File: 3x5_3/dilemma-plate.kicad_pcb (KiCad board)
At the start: 2 copper layers, 134 x 95.1 mm, 24 parts, among them SW101 NA_SW_Push, SW102 NA_SW_Push, SW103 NA_SW_Push, SW104 NA_SW_Push, SW105 NA_SW_Push, SW106 NA_SW_Push, SW107 NA_SW_Push, SW108 NA_SW_Push, SW109 NA_SW_Push, SW112 NA_SW_Push, SW113 NA_SW_Push, SW114 NA_SW_Push, SW115 NA_SW_Push, SW116 NA_SW_Push, SW117 NA_SW_Push, SW118 NA_SW_Push, SW119 NA_SW_Push, SW3001 NA_SW_Push

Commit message: switchplate
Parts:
- added H111: NA_Mount, local-libraries:Tenting_Puck, B.Cu at (168.8, 59.2)
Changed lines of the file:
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@@
 		)
 		(group ""
-			(members "18a6017f-ffb6-468c-8ad2-d1e65c980797" "1e9dc653-d796-481e-916b-10005a3d162f"
-				"1fd756a0-f206-4082-b7b1-289f6806d907" "298fd9b2-c9c4-4fb9-807c-0fc8cd5b9cba"
-				"35375497-e94a-4f06-a222-bf7addb77599" "3b888a55-3c4c-41de-9f1a-ac9d52ed99d5"
-				"3e25eb27-7766-4408-993b-eabdf33a15bf" "431225ac-bd0e-4e08-a494-c40d164e2537"
-				"522cac54-0b11-4791-888c-e7ded3e0ca3d" "522d6815-39b9-461e-8790-dd977ede2398"
-				"5546a2ae-57d7-40bc-8d2e-3e6342b024a3" "56fc0188-a46c-4fea-85be-565f00de21f7"
-				"5b26266e-9816-4449-ae28-c63e9d40efc1" "6105f4c5-8b0d-40ea-9fff-03a51df45137"
-				"62fa6b5c-3e7a-47ea-8490-97169fca3748" "6d991e6b-c12e-49aa-97fe-81406dea6a0f"
-				"77ab767f-daca-4994-b1dc-09e0116332ce" "783291f6-c796-4002-8fba-8e5e8cd6a844"
-				"8028d15d-6b94-4461-b460-0e59a82dbef8" "8036b940-5d2f-47a3-92ce-c59f15daa10a"
-				"827b9336-2005-4876-91df-0b7e21506845" "888ccea9-396c-47db-8d12-6a158d271942"
-				"95e2d21a-c768-495e-ab0f-7fdc0561792a" "963e86f8-8028-43a5-a583-777a1a724f63"
-				"9725a7eb-fbad-4445-997b-6893073f64e4" "97797248-1ebb-4d67-9d40-7fa9f49aa101"
-				"a31a874a-10a9-4085-bb2e-7ae6c695fd1d" "a3d442e0-a006-4df3-9afb-74bad3d9074a"
-				"a6783e92-1c61-4fac-9a5e-fdf22107ddb4" "a6edc55a-221d-4ae6-bffb-877fa3f8255f"
-				"ab6da59e-c0c9-444f-ac9c-b41e1cc33cb7" "b2584371-f3ef-4b80-afc1-b0a9ac187e03"
-				"b791176a-09aa-49ba-aaf0-00d4e364508e" "be3320bc-3aa9-4157-b558-ef6af8c43c2e"
-				"c70f1618-31fa-4ea9-8e51-2fd3c1244cda" "cbf11959-a461-4afa-af92-5fb8a755fd74"
-				"d0f27782-a812-427e-a1fb-0f6bc1eb0358" "d61a1469-8a70-457c-a318-8e3a44313dac"
-				"d95e60d4-b23c-42c9-b0ee-c09b32c68f8e" "dcc2c6ab-cf55-4ea2-81b9-2faa12349492"
-				"e28f69b4-e63c-443d-b198-09082df40ac6" "e9561920-4c84-434b-bb06-192ef4388cd0"
-				"f6fa60ae-145d-4918-8f28-a70c0320631c" "fc3d7266-24b8-47f1-844e-45b49a9f565e"
+			(members "06fd2d42-9e3d-4690-9213-9cdc7a998e4e" "1578d53f-b03b-43ed-a1ee-80c129b84bd2"
+				"237d5ba1-f081-4609-a567-8f08e89e4127" "28eae3de-9e28-4a41-8eb8-48b5cdd89c41"
+				"294e80ac-4184-4ab5-9341-ffd47eff33fc" "2975c91c-a03c-473c-bd74-390e810a9597"
+				"29f52380-fb83-4aa3-a89f-b73e0a496111" "305da9ae-5ffd-4334-9232-f78d5d0c655c"
+				"30b917aa-8564-41ad-8b33-177330258a9c" "3e56117d-53eb-4852-b9c6-79d85b387bfd"
+				"43157336-987f-4d6d-b473-97e6e7ea65f8" "474277ff-e58b-42ca-8847-5ec2961336b0"
+				"4b58b3f7-d579-4dae-9ab5-2eadcf436765" "4e783968-626b-453f-9e8c-af5ce592b87f"
+				"5e36adeb-0ae9-4595-8625-8b71ac3db49f" "64f87574-665c-4c55-b142-3479ecc681e7"
+				"7b14f2b2-a3c5-4c18-b87d-7dc452cad28d" "816d5be3-ad1d-4093-8293-c9ca824681f1"
+				"86f8b43b-9496-4e81-a316-fd0874fc5bbe" "8ac8b40f-5e56-4f93-b245-1ac4802ae0d8"
+				"8af15865-d14f-4799-94c6-4796ff3b591c" "8f9fe790-5dac-4837-b069-54cc2bed380f"
+				"a1de6a0e-e801-4096-9e97-b76ef23cf29b" "abce0806-6be1-4dff-baf0-25169a85b802"
+				"ac760ca8-94c7-4b5d-9ac1-3859706e7361" "b8b2ae66-e225-4aaf-9699-645195d9f203"
+				"bfe42b0a-a41d-4173-98ff-4e29ef4d0ce2" "c3fba9c8-64d9-4dd2-adaa-3e0f3d6c86c7"
+				"c610c947-f08c-4c62-9cae-8f4063d5ef53" "c62e7d53-a06d-43a2-968e-50d40d3d567e"
+				"cc202e0e-54ce-4020-a82c-725328c2bc64" "ce58a989-494d-4a23-89b7-83f7079ed86a"
+				"cfa665a7-74ce-4c42-aafe-aaeaebf58315" "d1dca15e-f5bd-4f12-9e30-401d0c6acb44"
+				"d2b790f4-0cd0-406d-80cc-713ac24b94a8" "de0415ec-40ee-4386-ac46-e22b8ec5d8ed"
+				"de9cb561-0bd9-449c-bda0-48421d41c01f" "e0de89f6-01da-4d33-8a33-5b12410997d6"
+				"eac9e065-d1d7-4c2d-8003-bac2994f45c2" "ee5158d9-56d6-4d14-989b-34b3a98f6705"
+				"f32ef78e-e253-4809-b456-d9da4f69ab00" "f3ebe4a0-9bb8-4ab5-9a76-b6f739c461e0"
+				"f572ede6-f1ac-4467-929a-14f66eda8436" "febe2a79-b729-4377-9e0e-fca7a02990ea"
 			)
 		)
 		(group ""
-			(members "09db1e25-32aa-4ef7-a801-1a4d3a7703aa" "1721c799-6c48-4b41-a06e-eb83d81ddd35"
-				"18695e2b-f4d1-4c85-97b2-719e40031901" "18f9db1f-c1aa-43d9-9a97-33acef636061"
-				"1a17ef04-b39a-41f3-bd05-5ed670e8d600" "219d5a18-44d3-4d0b-8c8f-8c2cd77120ba"
-				"27892d36-def2-42ac-9375-983866aa5da8" "27d40e2b-8d4c-41e4-9cff-be2816dc7aaf"
-				"2dca4c84-2a39-4120-91bd-9cd100300d82" "31e56cef-c40a-4116-b078-ee639f653285"
-				"3554aed6-744f-4598-9225-305823322764" "3b3830c3-175b-4431-ae89-d234977e23cd"
-				"3dd4ff90-4530-4ebb-8f0f-196ba7f41307" "4211f507-587d-44b1-bc27-00e7b932d8a3"
-				"45364870-d1d5-4007-97dd-f0691769606e" "4641e681-9294-41fe-adac-0f594359f7f6"
-				"4a5d3dad-004b-49e7-acd8-99cb7cd6b6a1" "51141ef9-e766-4350-b422-3ee6d5f9b46b"
-				"5e321f4e-2d66-43e3-90c1-286135b956e1" "5f832338-cb1d-4218-8020-77c02a538fb9"
-				"63e8c676-abf5-4142-a881-16bd1666c100" "689e09dd-37e6-45bb-a355-fe194fcbc5cc"
-				"68b40267-dcaa-49f4-b368-9ca4509b9f10" "691c8cd8-39c2-4433-8c8f-8faa07cb77be"
-				"7117dea3-892a-4464-8fd9-11fd78e307bb" "77f0d237-40b7-4d4a-af0e-c6f2ad87845f"
-				"7bc9859a-f086-4d82-a0a5-89f285ec93ef" "7fbba4e9-8cbf-407c-8054-986c5d681409"
-				"8613b2f2-5d7d-4724-ae6f-32ce31ccb30c" "86b14653-a136-49a9-826e-1232fba39c13"
-				"97f9e913-19fd-4681-ad5c-409789bf5f4e" "a0f5eea1-16b2-46d1-a3ec-58cb46950447"
-				"a2cf0c55-3d64-4f45-85ea-233774a8b215" "a68c6a4f-a56a-48f9-8601-1886f23db27f"
-				"b2b72eb8-ab92-478b-a4f5-4fbaade26284" "b6376346-ca1f-4beb-b848-6e822b6d98bc"
-				"bdbe05c0-a9d7-4596-95e5-625b7dd3a443" "d48d3277-666f-44d1-b974-c6cb9e085797"
-				"e4e94577-c601-474e-b480-d72cc8fa1aac" "e9b25dc9-ced6-43fc-a5bb-07762931e49d"
-				"ebadfb83-9592-43b6-a1a6-d65e71fdb965" "ed544ebf-7611-4475-aed8-4992a1cd33e7"
-				"f558f242-63b6-4c4e-9f58-8ea8db819fcc" "f6faec9d-3fe0-4362-89e2-a19bac4138ea"
+			(members "023f1531-cdb9-4fec-bc1c-30b353bbd425" "05eeaacc-d00a-49bb-9701-68f7cc664f99"
+				"06ee38d9-5cc6-4e51-9b35-590467cde55b" "0caf612b-0f2e-4e23-849f-4ddd47a9421c"
+				"20920631-cbf3-45aa-b9e3-f41fb86d794a" "252897e3-89eb-416f-ba69-3616c9e3b792"
+				"253a56cc-ad2a-412e-aef9-b3c77c0f458a" "294e8c06-04b6-4a5a-8521-8000344e3dd5"
+				"2aad696d-7504-43ed-876d-4556a7ee225a" "31e1b6f0-88c4-4084-b999-a8423be61ef4"
+				"39cbe460-93ce-42d5-a08b-2a2e03090798" "3f090ea8-7917-4c1a-b98f-d837dc72604a"
+				"453914ab-59a3-450e-9a61-e80d0552d3a4" "4c2215bc-913a-47b4-bc5c-8458a14d10cb"
+				"515815b8-4a05-44f4-865c-4849c54064bd" "56106be6-5a14-4053-bc46-669d98b8174c"
+				"59b2c7ef-d19f-42cd-967e-0b37358fa4e2" "6532f12f-924f-45f7-9983-fd1916e48f4d"
+				"717bc7cc-0da1-4a1f-9089-1a8f8f21f463" "72e33b98-1de1-464b-8bee-755099197c92"
+				"7420bbcf-6ea1-475d-8ac1-63097aa65ce1" "7c256379-28db-4036-b6c7-5a121d062823"
+				"821bd146-9e21-418e-8531-a5ff9f92b814" "910f03dc-7432-424e-8432-405fda47f710"
+				"a1155585-1d5f-43b1-a4ad-5bb6ee82f6f9" "a4dde7f3-fa00-4768-81c7-4b4e9916be64"
+				"abeebf3b-9cde-495c-b038-1ac87fe764fc" "ad29b3c5-68e1-4fde-9614-e4644f444a64"
+				"aed007e6-9b76-4a0f-bb32-adb0a0579cf1" "b3d8db52-21fe-4db5-9d41-86a5c0d2fe50"
+				"b7c0ddd1-2889-497d-a21e-54b68900bbed" "bed90bb8-b6dc-4465-a854-73c4ac9a7540"
+				"bfe1c718-9d7e-4a9b-aab4-7e6f4041f74b" "d032343c-2f3d-459d-9b51-0ee7d33156c8"
+				"d5f5c844-7438-489e-83d5-e8965c85bd03" "d9d50360-718d-4724-b588-1d28dec1b1d0"
+				"dc2dc6bd-9625-41aa-a7ca-04fa0e545d7c" "dffb0c17-2d36-4ecd-ba2a-03365fb7a4e7"
+				"ea620fb0-fd8a-4be9-8e5e-c29c7e2c56e2" "ebd71274-7b5c-4eb0-98a8-951ff513c528"
+				"f0a61849-0228-4710-a1ab-4a20659c4b5a" "f1484936-3e9b-4934-a5f1-1feb71b5591a"
+				"f579663f-bfaf-4b16-8c4e-1b1a97475be1" "fd368f95-2342-4ec1-9e2e-ad86804587fc"
 			)
 		)
@@
 		)
 	)
+	(footprint "local-libraries:Tenting_Puck"
+		(layer "B.Cu")
+		(at 168.828808 59.1825 180)
+		(property "Reference" "H111"
+			(at 7.6835 -1.4605 180)
+			(layer "B.Fab")
+			(effects
+				(font
+					(size 1 1)
+					(thickness 0.15)
+				)
+				(justify mirror)
+			)
+		)
+		(property "Value" "NA_Mount"
+			(at 8.0645 2.8575 180)
+			(layer "B.Fab")
+			(effects
+				(font
+					(size 1 1)
+					(thickness 0.15)
+				)
+				(justify mirror)
+			)
+		)
+		(property "Footprint" "local-libraries:Tenting_Puck"
+			(at 0 0 0)
+			(unlocked yes)
+			(layer "B.Fab")
+			(hide yes)
+			(effects
+				(font
+					(size 1.27 1.27)
+				)
+				(justify mirror)
+			)
+		)
+		(property "Datasheet" ""
+			(at 0 0 0)
+			(unlocked yes)
+			(layer "B.Fab")
+			(hide yes)
+			(effects
+				(font
+					(size 1.27 1.27)
+				)
+				(justify mirror)
+			)
+		)
+		(property "Description" ""
+			(at 0 0 0)
+			(unlocked yes)
+			(layer "B.Fab")
+			(hide yes)
+			(effects
+				(font
+					(size 1.27 1.27)
+				)
+				(justify mirror)
+			)
+		)
+		(property ki_fp_filters "MountingHole*Pad*")
+		(sheetname "Root")
+		(sheetfile "dilemma.kicad_sch")
+		(attr through_hole exclude_from_pos_files)
+		(fp_circle
+			(center 19.05 0)
+			(end 21.159502 0)
+			(stroke
+				(width 0.05)
+				(type default)
+			)
+			(fill none)
+			(layer "Edge.Cuts")
+		)
+		(fp_circle
+			(center 0 19.05)
+			(end 2.109502 19.05)
+			(stroke
+				(width 0.05)
+				(type default)
+			)
+			(fill none)
+			(layer "Edge.Cuts")
+		)
+		(fp_circle
+			(center 0 -19.05)
+			(end 2.109502 -19.05)
+			(stroke
+				(width 0.05)
+				(type default)
+			)
+			(fill none)
+			(layer "Edge.Cuts")
+		)
+		(fp_circle
+			(center -19.05 0)
+			(end -16.940498 0)
+			(stroke
+				(width 0.05)
+				(type default)
+			)
+			(fill none)
+			(layer "Edge.Cuts")
+		)
+		(fp_circle
+			(center 0 0)
+			(end 20.55 0)
+			(stroke
+				(width 0.55)
+				(type solid)
+			)
+			(fill none)
+			(layer "F.CrtYd")
+		)
+	)

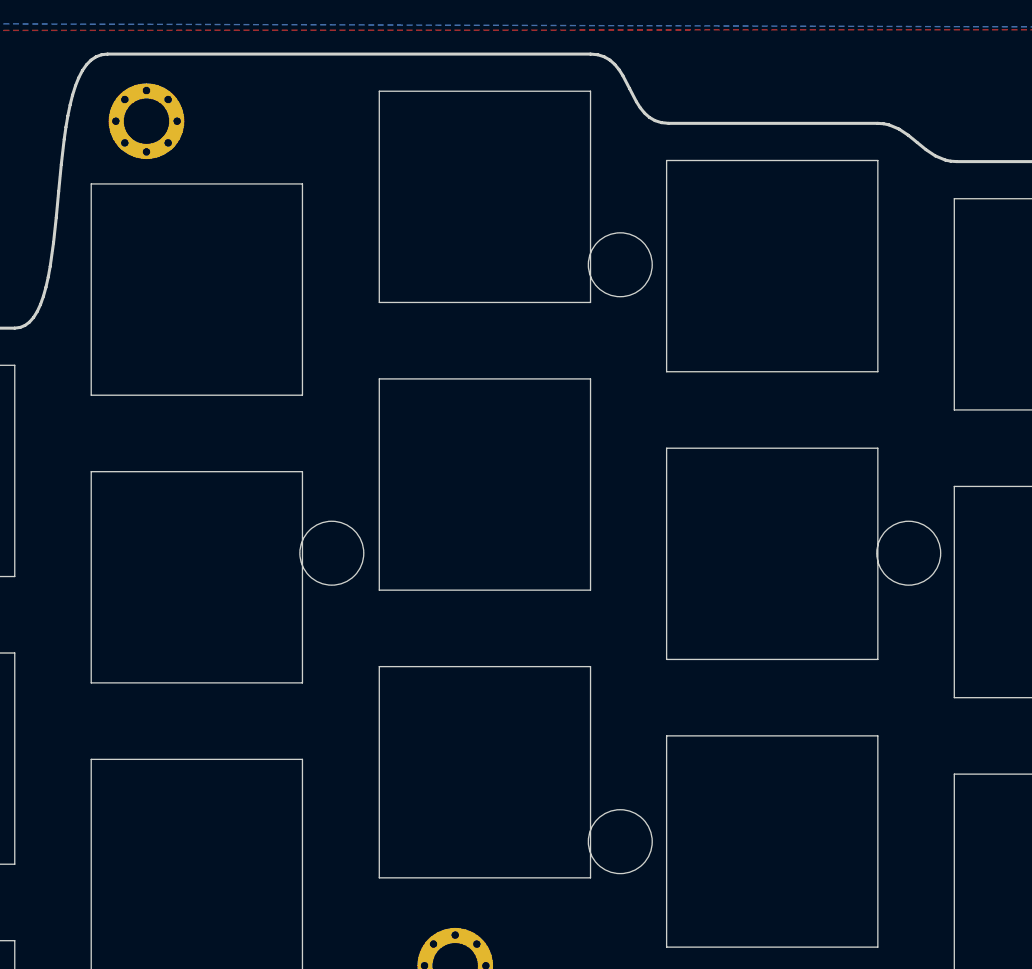
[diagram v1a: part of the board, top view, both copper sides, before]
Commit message: add puck screw cutouts
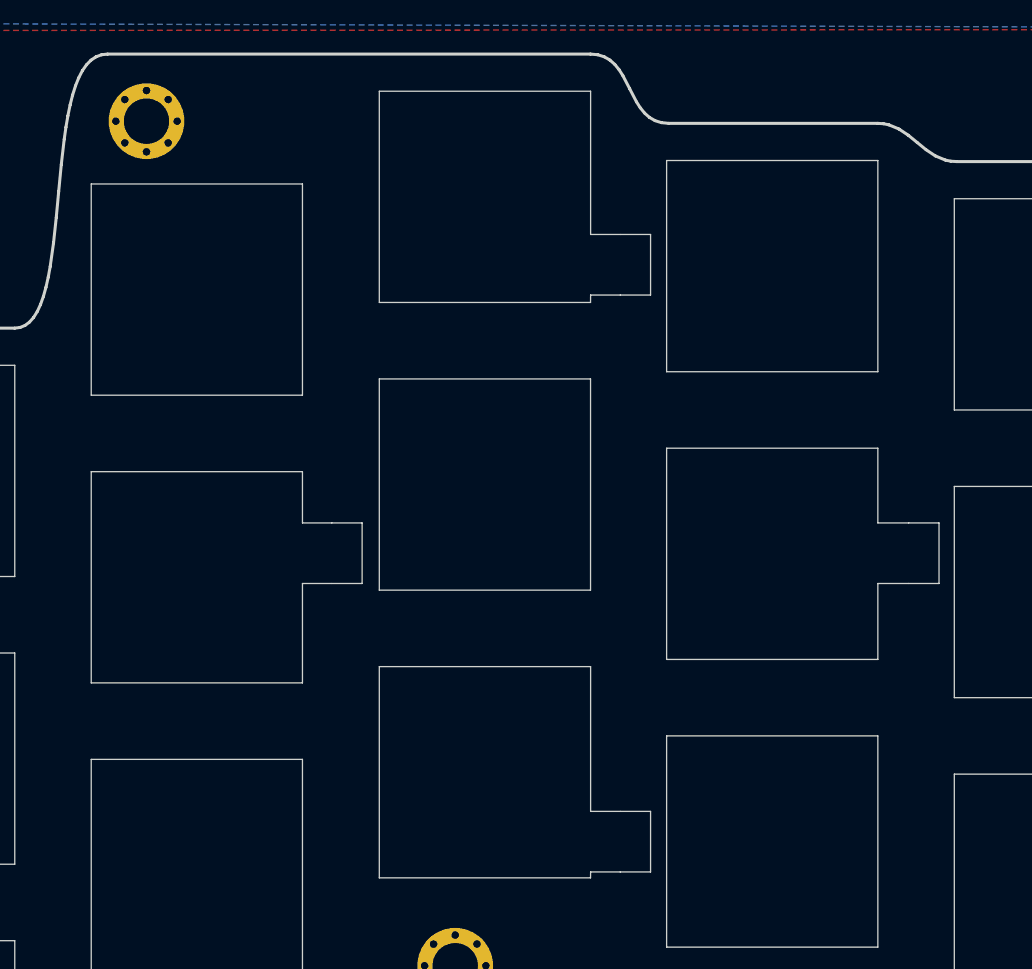
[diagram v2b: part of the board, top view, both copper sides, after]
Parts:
- removed H111: NA_Mount, local-libraries:Tenting_Puck
- removed SW105, SW107, SW109, SW113: NA_SW_Push, local-libraries:SW_Kailh_Choc_V2_1.00u_plate_cutout
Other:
- outline, holes or cut-outs redrawn
